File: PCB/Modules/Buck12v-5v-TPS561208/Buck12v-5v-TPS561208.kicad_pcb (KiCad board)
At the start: 2 copper layers, 42.7 x 25.2 mm, 8 parts, among them U1 TPS561208DDCT

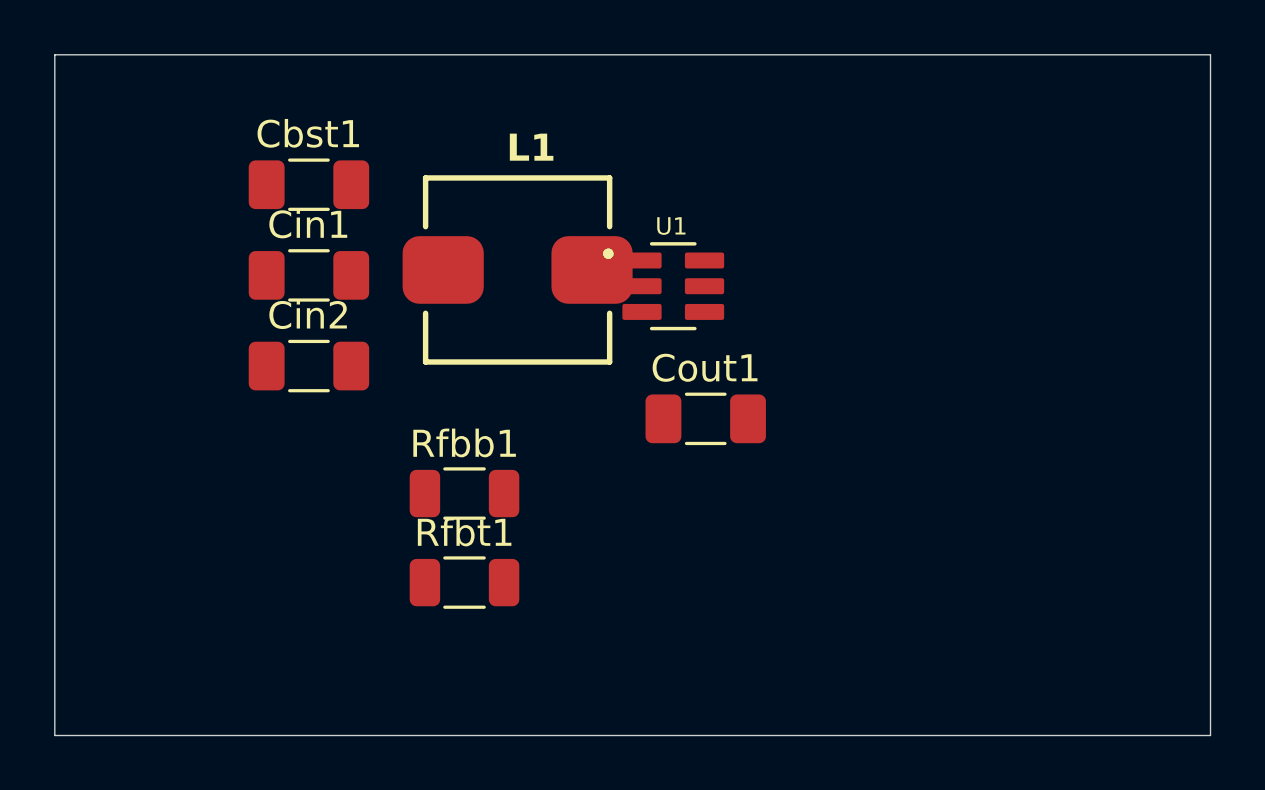
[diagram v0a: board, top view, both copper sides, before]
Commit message: Added buck design
Signed-off-by: Simonca Raul <simonca.raul@gmail.com>
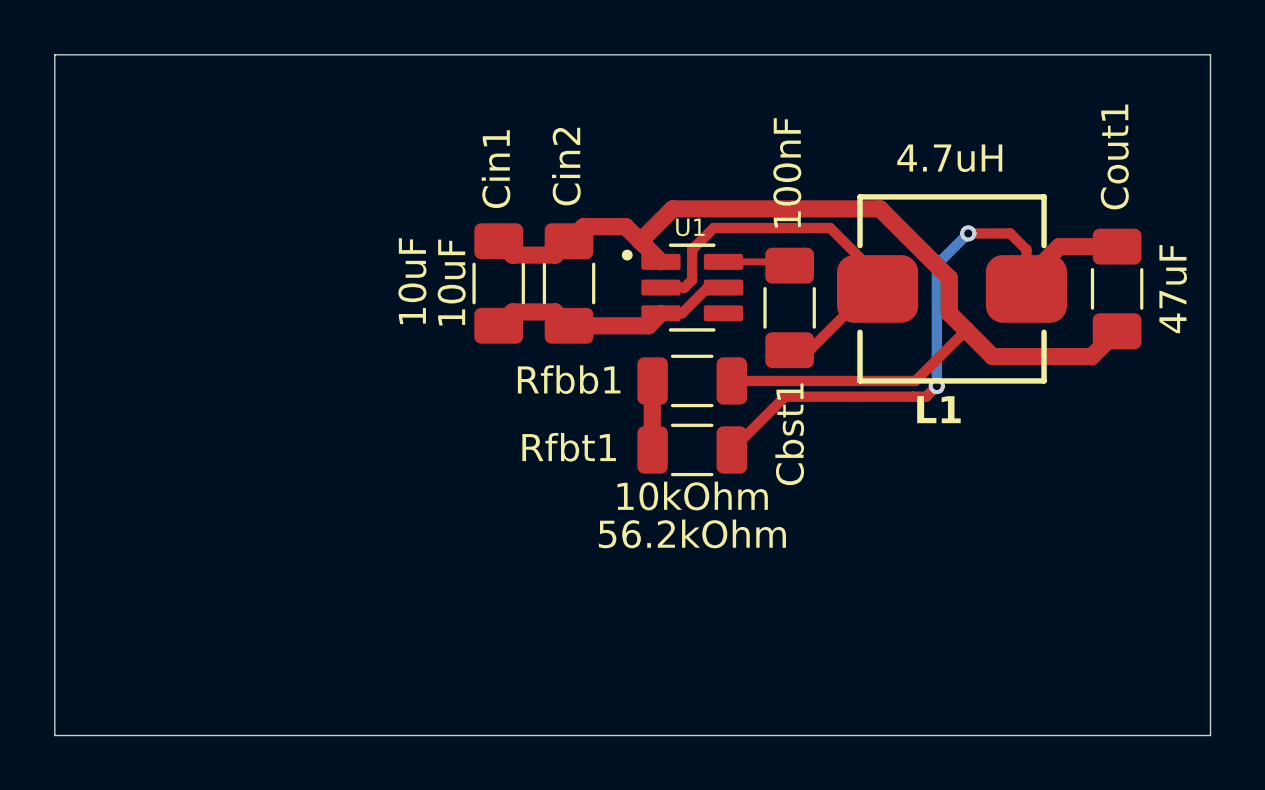
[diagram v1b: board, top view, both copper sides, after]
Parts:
- moved Cbst1 18.3 mm to (159.4, 89.4), turned to -90 degrees
- moved L1 16.1 mm to (165.4, 88.7), turned to 180 degrees
- moved Cout1 15.9 mm to (171.6, 88.7), turned to -90 degrees
- moved Cin2 10.1 mm to (151.3, 88.5), turned to 90 degrees
- moved Rfbt1 9.74 mm to (155.8, 94.7), turned to 180 degrees
- moved Rfbb1 9.38 mm to (155.8, 92.1)
- moved Cin1 7.02 mm to (148.7, 88.5), turned to 90 degrees
- moved U1 0.70 mm to (155.8, 88.7)
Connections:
- net Net-(U1-SW) renamed /SW
- net Net-(U1-VBST) renamed /VBST
- net Net-(U1-VFB) renamed /VFB
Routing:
- net GND: track 0.00 -> 38.1 mm
- net +5V: track 0.00 -> 22.8 mm, vias 0 -> 2
- net /SW: track 0.00 -> 15.3 mm
- net +12V: track 0.00 -> 9.31 mm
- net /VBST: track 0.00 -> 2.62 mm
- net /VFB: track 0.00 -> 2.60 mm

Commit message: Added new components and modules
Signed-off-by: Simonca Raul <simonca.raul@gmail.com>
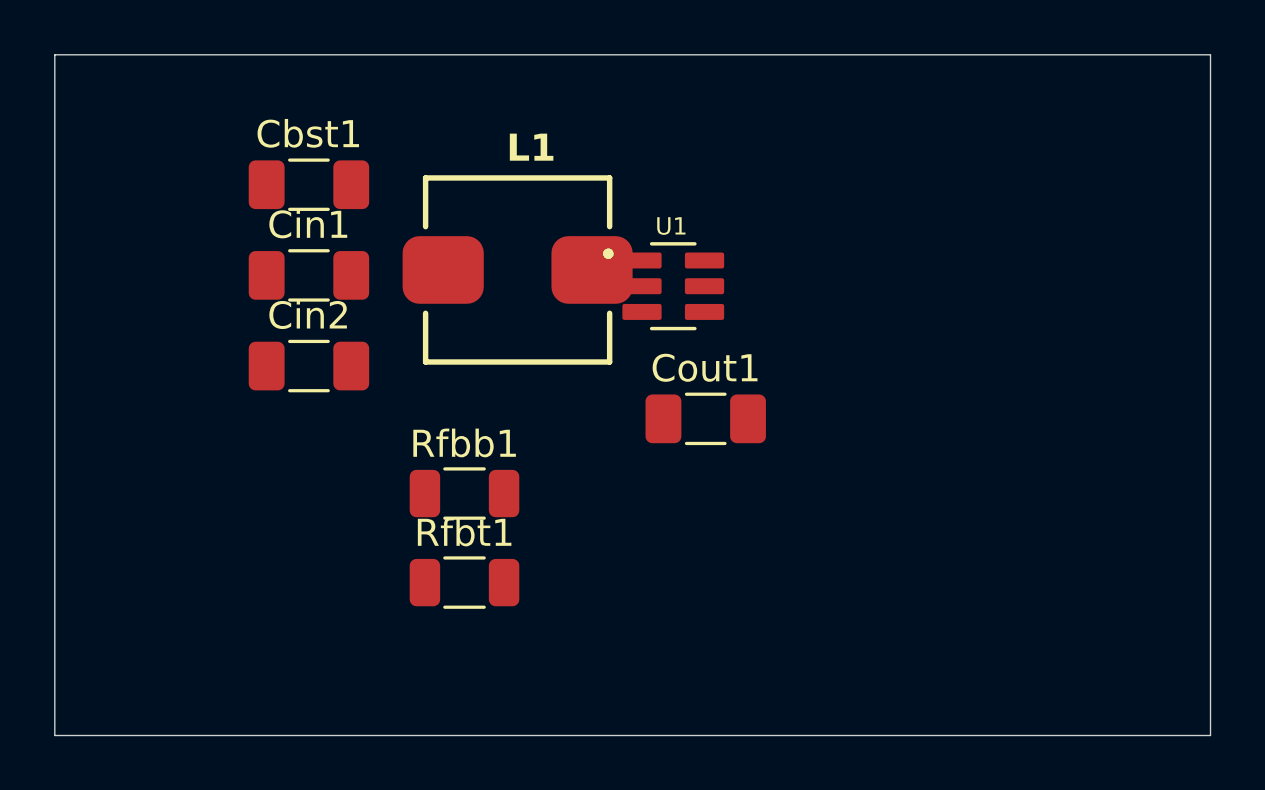
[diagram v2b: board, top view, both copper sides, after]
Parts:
- moved Cbst1 18.3 mm to (141.7, 84.8), turned to 0 degrees
- moved L1 16.1 mm to (149.4, 88.0), turned to 0 degrees
- moved Cout1 15.9 mm to (156.3, 93.5), turned to 0 degrees
- moved Cin2 10.1 mm to (141.7, 91.5), turned to 0 degrees
- moved Rfbt1 9.74 mm to (147.4, 99.5), turned to 0 degrees
- moved Rfbb1 9.38 mm to (147.4, 96.3)
- moved Cin1 7.02 mm to (141.7, 88.2), turned to 0 degrees
- moved U1 0.70 mm to (155.2, 88.6)
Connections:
- net /SW renamed Net-(U1-SW)
- net /VBST renamed Net-(U1-VBST)
- net /VFB renamed Net-(U1-VFB)
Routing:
- net GND: track 38.1 -> 0.00 mm
- net +5V: track 22.8 -> 0.00 mm, vias 2 -> 0
- net Net-(U1-SW): track 15.3 -> 0.00 mm
- net +12V: track 9.31 -> 0.00 mm
- net Net-(U1-VBST): track 2.62 -> 0.00 mm
- net Net-(U1-VFB): track 2.60 -> 0.00 mm
